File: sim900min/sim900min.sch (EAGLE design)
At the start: 2 parts

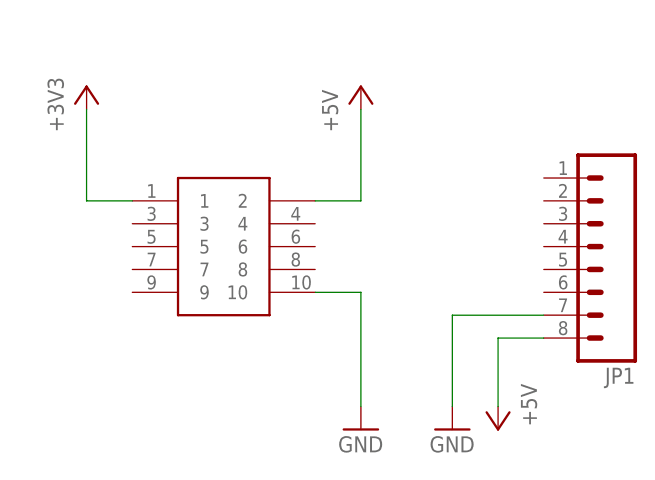
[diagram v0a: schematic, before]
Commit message: redesigned sim900min for pcb production
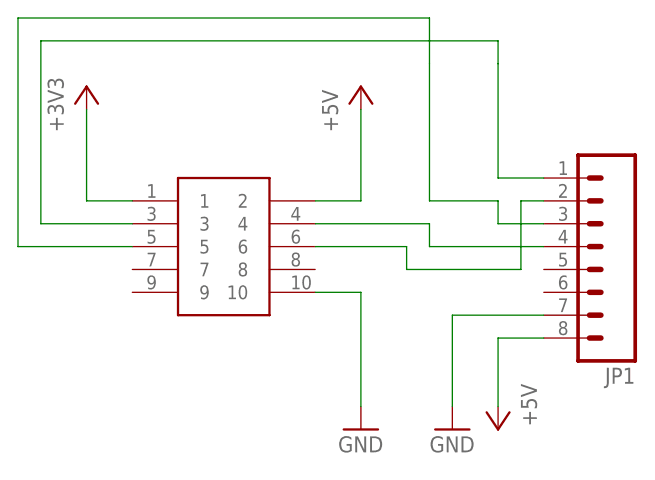
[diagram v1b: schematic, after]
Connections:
- new net N$2: JP1.4, U$1.4
- new net N$3: JP1.3, U$1.5
- new net N$4: JP1.2, U$1.6
- new net N$5: JP1.1, U$1.3
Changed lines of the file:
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@@
 </classes>
 <parts>
-<part name="U$1" library="ozlollc" deviceset="SHF105" device="SM"/>
 <part name="JP1" library="SparkFun-Connectors" deviceset="M08" device="1X08"/>
 <part name="P+1" library="supply1" deviceset="+5V" device=""/>
@@
 <part name="GND2" library="supply1" deviceset="GND" device=""/>
 <part name="+3V1" library="supply1" deviceset="+3V3" device=""/>
+<part name="U$1" library="ozlollc" deviceset="SHF105" device="SM"/>
 </parts>
 <sheets>
@@
 </plain>
 <instances>
-<instance part="U$1" gate="X" x="50.8" y="50.8"/>
 <instance part="JP1" gate="G$1" x="91.44" y="50.8" rot="R180"/>
 <instance part="P+1" gate="1" x="66.04" y="68.58"/>
@@
 <instance part="GND2" gate="1" x="76.2" y="30.48"/>
 <instance part="+3V1" gate="G$1" x="35.56" y="68.58"/>
+<instance part="U$1" gate="X" x="50.8" y="50.8"/>
 </instances>
 <busses>
@@
 <net name="+3V3" class="0">
 <segment>
-<pinref part="U$1" gate="X" pin="1"/>
 <pinref part="+3V1" gate="G$1" pin="+3V3"/>
 <wire x1="40.64" y1="55.88" x2="35.56" y2="55.88" width="0.1524" layer="91"/>
 <wire x1="35.56" y1="55.88" x2="35.56" y2="66.04" width="0.1524" layer="91"/>
+<pinref part="U$1" gate="X" pin="1"/>
 </segment>
 </net>
 <net name="+5V" class="0">
 <segment>
-<pinref part="U$1" gate="X" pin="2"/>
 <pinref part="P+1" gate="1" pin="+5V"/>
 <wire x1="60.96" y1="55.88" x2="66.04" y2="55.88" width="0.1524" layer="91"/>
 <wire x1="66.04" y1="55.88" x2="66.04" y2="66.04" width="0.1524" layer="91"/>
+<pinref part="U$1" gate="X" pin="2"/>
 </segment>
 <segment>
@@
 <net name="GND" class="0">
 <segment>
-<pinref part="U$1" gate="X" pin="10"/>
 <pinref part="GND1" gate="1" pin="GND"/>
 <wire x1="60.96" y1="45.72" x2="66.04" y2="45.72" width="0.1524" layer="91"/>
 <wire x1="66.04" y1="45.72" x2="66.04" y2="33.02" width="0.1524" layer="91"/>
+<pinref part="U$1" gate="X" pin="10"/>
 </segment>
 <segment>
@@
 </segment>
 </net>
+<net name="N$2" class="0">
+<segment>
+<wire x1="60.96" y1="53.34" x2="73.66" y2="53.34" width="0.1524" layer="91"/>
+<wire x1="73.66" y1="53.34" x2="73.66" y2="50.8" width="0.1524" layer="91"/>
+<pinref part="JP1" gate="G$1" pin="4"/>
+<wire x1="73.66" y1="50.8" x2="86.36" y2="50.8" width="0.1524" layer="91"/>
+<pinref part="U$1" gate="X" pin="4"/>
+</segment>
+</net>
+<net name="N$3" class="0">
+<segment>
+<wire x1="40.64" y1="50.8" x2="27.94" y2="50.8" width="0.1524" layer="91"/>
+<wire x1="27.94" y1="50.8" x2="27.94" y2="76.2" width="0.1524" layer="91"/>
+<wire x1="27.94" y1="76.2" x2="73.66" y2="76.2" width="0.1524" layer="91"/>
+<wire x1="73.66" y1="76.2" x2="73.66" y2="71.12" width="0.1524" layer="91"/>
+<wire x1="73.66" y1="71.12" x2="73.66" y2="55.88" width="0.1524" layer="91"/>
+<wire x1="73.66" y1="55.88" x2="81.28" y2="55.88" width="0.1524" layer="91"/>
+<wire x1="81.28" y1="55.88" x2="81.28" y2="53.34" width="0.1524" layer="91"/>
+<pinref part="JP1" gate="G$1" pin="3"/>
+<wire x1="81.28" y1="53.34" x2="86.36" y2="53.34" width="0.1524" layer="91"/>
+<pinref part="U$1" gate="X" pin="5"/>
+</segment>
+</net>
+<net name="N$4" class="0">
+<segment>
+<wire x1="60.96" y1="50.8" x2="71.12" y2="50.8" width="0.1524" layer="91"/>
+<wire x1="71.12" y1="50.8" x2="71.12" y2="48.26" width="0.1524" layer="91"/>
+<wire x1="71.12" y1="48.26" x2="83.82" y2="48.26" width="0.1524" layer="91"/>
+<wire x1="83.82" y1="48.26" x2="83.82" y2="55.88" width="0.1524" layer="91"/>
+<pinref part="JP1" gate="G$1" pin="2"/>
+<wire x1="83.82" y1="55.88" x2="86.36" y2="55.88" width="0.1524" layer="91"/>
+<pinref part="U$1" gate="X" pin="6"/>
+</segment>
+</net>
+<net name="N$5" class="0">
+<segment>
+<wire x1="40.64" y1="53.34" x2="30.48" y2="53.34" width="0.1524" layer="91"/>
+<wire x1="30.48" y1="53.34" x2="30.48" y2="73.66" width="0.1524" layer="91"/>
+<wire x1="30.48" y1="73.66" x2="81.28" y2="73.66" width="0.1524" layer="91"/>
+<wire x1="81.28" y1="73.66" x2="81.28" y2="71.12" width="0.1524" layer="91"/>
+<wire x1="81.28" y1="71.12" x2="81.28" y2="58.42" width="0.1524" layer="91"/>
+<pinref part="JP1" gate="G$1" pin="1"/>
+<wire x1="81.28" y1="58.42" x2="86.36" y2="58.42" width="0.1524" layer="91"/>
+<pinref part="U$1" gate="X" pin="3"/>
+</segment>
+</net>
